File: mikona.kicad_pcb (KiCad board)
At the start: 4 copper layers, 50 x 40 mm, 66 parts, among them J1 TC2030-IDC-NL, Q1 BSC109N10NS3G, Q2 STN3N40K3, Q3 IGB50N65S, Q4 IGB50N65S, Q5 BSS138, U1 LT3750EMSTR, U2 ZXGD3009E6, U3 NCS325, U4 PIC16F15224, U5 IX4427MTR, U8 AP63203WU

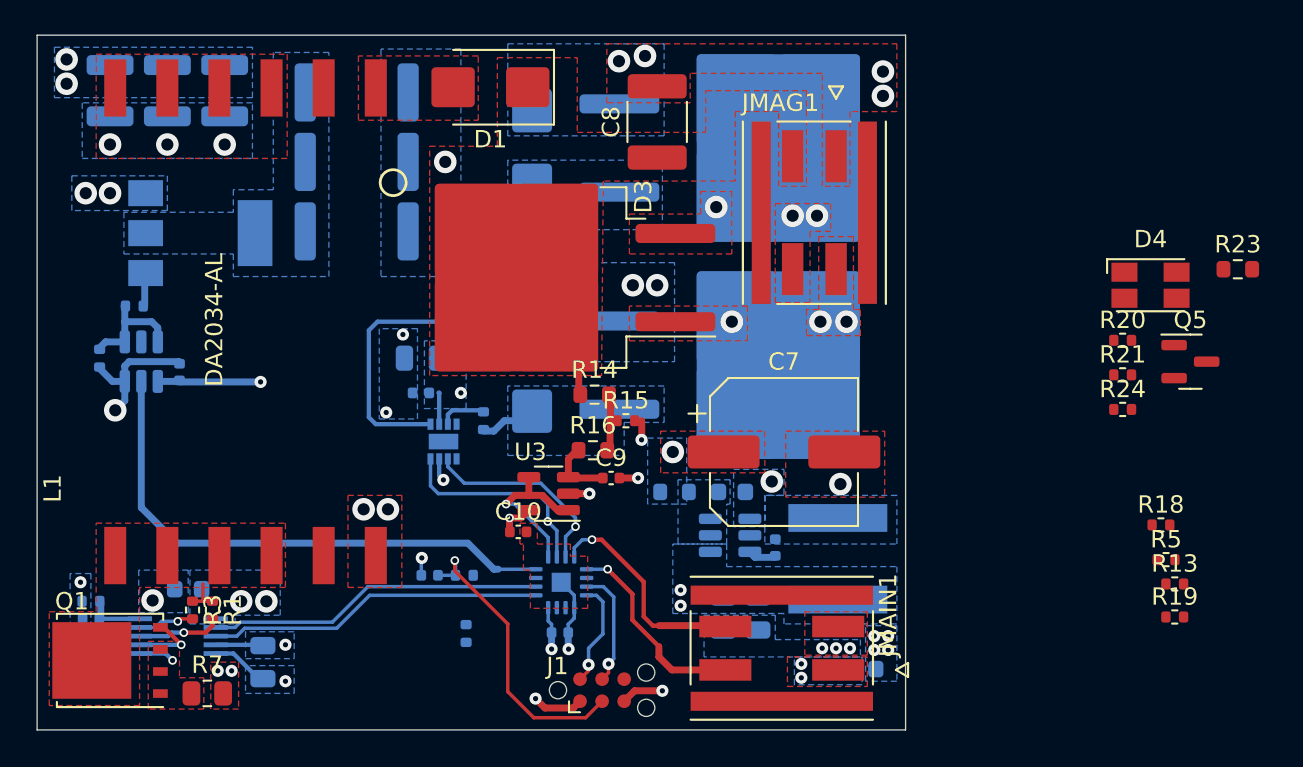
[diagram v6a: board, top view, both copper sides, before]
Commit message: Finish routing.
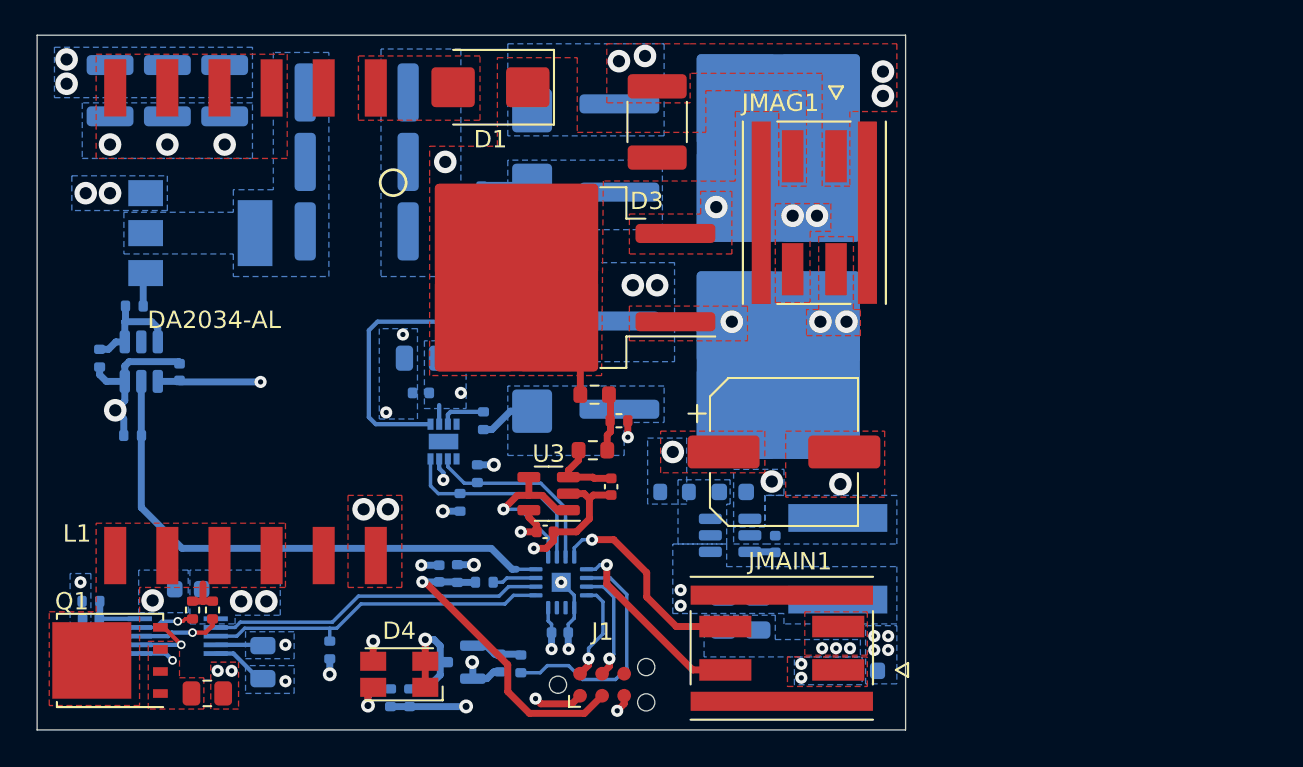
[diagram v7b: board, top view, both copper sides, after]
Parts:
- Q5, R13, R18, R19, R20, R21, R24, R5: moved to B.Cu
- R23: value 0 -> 100; footprint Resistor_SMD:R_0603_1608Metric -> Resistor_SMD:R_0402_1005Metric; moved to B.Cu
- moved R18 59.4 mm to (129.0, 108.0)
- moved D4 48.7 mm to (144.3, 121.8), turned to 180 degrees
- moved R19 48.7 mm to (140.3, 120.4), turned to 90 degrees
- moved R23 47.1 mm to (151.3, 121.2), turned to -90 degrees
- moved R20 46.9 mm to (143.8, 123.2), turned to -90 degrees
- moved Q5 45.7 mm to (147.7, 121.1), turned to 180 degrees
- moved R21 45.1 mm to (144.9, 123.2), turned to -90 degrees
- moved R13 41.4 mm to (147.8, 111.9), turned to 90 degrees
- moved R5 40.0 mm to (148.8, 110.2), turned to -90 degrees
- moved R24 38.7 mm to (150.2, 121.2), turned to 90 degrees
- moved R2 3.49 mm to (147.7, 116.0)
- moved C10 1.55 mm to (152.8, 113.6)
- moved R22 1.22 mm to (149.2, 116.5)
- moved R17 0.60 mm to (149.1, 94.2)
- moved C11 0.56 mm to (146.7, 116.0), turned to -90 degrees
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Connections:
- R23 pad 1: /Logic/LED -> Net-(Q5-G)
- R23 pad 2: Net-(Q5-G) -> /Logic/LED
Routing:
- net /Logic/LED: track 0.00 -> 13.8 mm
- net GND: track 25.3 -> 38.2 mm, vias 32 -> 37
- net Net-(D4-A1): track 0.00 -> 7.53 mm, vias 0 -> 1
- net +3.3V: track 7.54 -> 13.0 mm, vias 5 -> 7
- net Net-(D4-K1): track 0.00 -> 3.19 mm, vias 0 -> 1
- net Net-(Q5-G): track 0.00 -> 2.99 mm
- net Net-(U4-RA3/~{MCLR}/VPP): track 0.00 -> 2.56 mm
- net /Logic/SW_NRST: track 17.1 -> 17.9 mm
- net /Logic/CHARGE: track 19.4 -> 20.1 mm
- net +24V: track 11.0 -> 10.3 mm
- net Net-(U5-OUT_B): track 21.1 -> 21.8 mm
- net Net-(U3-+): track 3.67 -> 4.28 mm
- net /Logic/KICK_A: track 11.5 -> 11.0 mm, vias 1 -> 0
- net /Logic/KICK_B: vias 1 -> 0
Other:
- board text added: "V.2023.0.4"
- board text removed: "V.2023.0.3"

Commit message: Minor fixes to the PCB.
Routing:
- net Net-(Q1-G): track 4.00 -> 5.43 mm
- net GND: track 38.2 -> 38.3 mm, vias 37 -> 38
